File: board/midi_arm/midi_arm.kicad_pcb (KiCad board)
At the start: 2 copper layers, 100 x 100 mm, 25 parts, among them J1 Conn_01x02_Pin, J2 Conn_01x02_Pin, J3 Conn_01x10_Pin, J4 RJ45, J5 Conn_01x03_Pin, J6 Conn_01x03_Pin, J7 Conn_01x03_Pin, U6 6DOF_6050

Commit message: BABOI 2.0 Board
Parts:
- removed C1, C2, C3: 100nF, Capacitor_SMD:C_01005_0402Metric
- removed U2, U3, U4: ~, midi_arm:TOUCH_BAR
- added H7: MountingHole, MountingHole:MountingHole_2.2mm_M2, F.Cu at (127.5, 27.5)
- added H8: MountingHole, MountingHole:MountingHole_2.2mm_M2, F.Cu at (154.5, 27.5)
- added J10: Conn_01x01_Pin, Connector_PinHeader_1.27mm:PinHeader_1x01_P1.27mm_Vertical, F.Cu at (134.9, 47.5)
- added J8: Conn_01x06_Pin, GPB_Footprints:JST_1x6_2.54_cablepad, B.Cu at (134.8, 66.6)
- added J9: Conn_01x01_Pin, Connector_PinHeader_1.27mm:PinHeader_1x01_P1.27mm_Vertical, F.Cu at (131.6, 31.2)
- added R1: 2.4k, Resistor_SMD:R_0805_2012Metric_Pad1.20x1.40mm_HandSolder, B.Cu at (146.3, 37.5)
- added R10: 24k, Resistor_SMD:R_0805_2012Metric_Pad1.20x1.40mm_HandSolder, B.Cu at (148.3, 50.5)
- added R11: 2.4k, Resistor_SMD:R_0805_2012Metric_Pad1.20x1.40mm_HandSolder, B.Cu at (131.1, 37.3)
- added R12: 2.4k, Resistor_SMD:R_0805_2012Metric_Pad1.20x1.40mm_HandSolder, B.Cu at (128.9, 37.3)
- added R13: 2.4k, Resistor_SMD:R_0805_2012Metric_Pad1.20x1.40mm_HandSolder, B.Cu at (126.7, 37.3)
- added R14: 2.4k, Resistor_SMD:R_0805_2012Metric_Pad1.20x1.40mm_HandSolder, B.Cu at (133.3, 37.3)
- added R15: 24k, Resistor_SMD:R_0805_2012Metric_Pad1.20x1.40mm_HandSolder, B.Cu at (135.6, 37.3)
- added R16: 2.4k, Resistor_SMD:R_0805_2012Metric_Pad1.20x1.40mm_HandSolder, B.Cu at (133.6, 44.3)
- added R17: 2.4k, Resistor_SMD:R_0805_2012Metric_Pad1.20x1.40mm_HandSolder, B.Cu at (133.7, 50.7)
- added R18: 2.4k, Resistor_SMD:R_0805_2012Metric_Pad1.20x1.40mm_HandSolder, B.Cu at (126.9, 47.4)
- added R19: 2.4k, Resistor_SMD:R_0805_2012Metric_Pad1.20x1.40mm_HandSolder, B.Cu at (125.9, 44.5)
- added R2: 2.4k, Resistor_SMD:R_0805_2012Metric_Pad1.20x1.40mm_HandSolder, B.Cu at (155.5, 37.5)
- added R20: 24k, Resistor_SMD:R_0805_2012Metric_Pad1.20x1.40mm_HandSolder, B.Cu at (126.0, 50.5)
- added R3: 2.4k, Resistor_SMD:R_0805_2012Metric_Pad1.20x1.40mm_HandSolder, B.Cu at (148.5, 37.5)
- added R4: 2.4k, Resistor_SMD:R_0805_2012Metric_Pad1.20x1.40mm_HandSolder, B.Cu at (153.1, 37.5)
- added R5: 24k, Resistor_SMD:R_0805_2012Metric_Pad1.20x1.40mm_HandSolder, B.Cu at (150.8, 37.5)
- added R6: 2.4k, Resistor_SMD:R_0805_2012Metric_Pad1.20x1.40mm_HandSolder, B.Cu at (155.8, 50.6)
- added R7: 2.4k, Resistor_SMD:R_0805_2012Metric_Pad1.20x1.40mm_HandSolder, B.Cu at (154.9, 47.4)
- added R8: 2.4k, Resistor_SMD:R_0805_2012Metric_Pad1.20x1.40mm_HandSolder, B.Cu at (155.9, 44.4)
- added R9: 2.4k, Resistor_SMD:R_0805_2012Metric_Pad1.20x1.40mm_HandSolder, B.Cu at (148.3, 44.3)
- added RV1: R_Potentiometer_Small, midi_arm:pot_9.5x9.5, F.Cu at (137.4, 47.5)
- added RV2: R_Potentiometer_Small, midi_arm:pot_9.5x9.5, F.Cu at (141.0, 38.1)
- added RV3: R_Potentiometer_Small, midi_arm:pot_9.5x9.5, F.Cu at (144.5, 47.5)
- added RV4: R_Potentiometer_Small, midi_arm:pot_9.5x9.5, F.Cu at (141.0, 29.0)
- added SW1: SW_MEC_5E, GPB_Footprints:switch_Touchpad, F.Cu at (161.8, 38.6)
- added SW2: SW_MEC_5E, GPB_Footprints:switch_Touchpad, F.Cu at (161.8, 55.1)
- added SW3: SW_MEC_5E, GPB_Footprints:switch_Touchpad, F.Cu at (181.1, 38.6)
- added SW4: SW_MEC_5E, GPB_Footprints:switch_Touchpad, F.Cu at (181.1, 55.1)
- added U8: ~, midi_arm:ADS1115_mod, F.Cu at (124.6, 64.0)
- added U9: ~, Package_DIP:DIP-8_W7.62mm, F.Cu at (134.4, 33.8)
- J1: value Conn_01x02_Pin -> Conn_01x06_Pin; footprint Connector_PinHeader_2.54mm:PinHeader_1x02_P2.54mm_Vertical -> GPB_Footprints:JST_1x6_2.54
- J2: value Conn_01x02_Pin -> Conn_01x03_Pin; footprint Connector_PinHeader_2.54mm:PinHeader_1x02_P2.54mm_Vertical -> midi_arm:LED_conn; moved to B.Cu
- J3: value Conn_01x10_Pin -> Conn_01x08_Pin; footprint Connector_PinHeader_2.54mm:PinHeader_1x10_P2.54mm_Vertical -> Connector_PinHeader_2.54mm:PinHeader_1x08_P2.54mm_Vertical
- J4: value RJ45 -> Conn_01x05_Pin; footprint Connector_RJ:RJ45_Ninigi_GE -> GPB_Footprints:JST_1x5_2.54_cablepad; moved to B.Cu
- J5, J6, J7: value Conn_01x03_Pin -> Conn_01x01_Pin; footprint Connector_PinHeader_2.54mm:PinHeader_1x03_P2.54mm_Vertical -> Connector_PinHeader_1.27mm:PinHeader_1x01_P1.27mm_Vertical
- U1: footprint midi_arm:Wemos_S3_Mini_Outer_Pins -> GPB_Footprints:ESP32_S2_Wemos_Mini
- U7: footprint midi_arm:TOUCH_BAR -> Package_DIP:DIP-8_W7.62mm
- moved H2 98.6 mm to (187.5, 27.5)
- moved H4 98.4 mm to (187.5, 122.5)
- moved H6 61.1 mm to (127.5, 70.4)
- moved U7 44.2 mm to (147.6, 41.4), turned to 90 degrees
- moved J1 43.3 mm to (180.3, 26.7), turned to -90 degrees
- moved U6 36.4 mm to (138.7, 53.8)
- moved J5 36.1 mm to (129.2, 53.7)
- moved J4 35.0 mm to (146.1, 31.4), turned to 90 degrees
- moved H1 33.6 mm to (160.6, 27.5)
- moved D2 31.1 mm to (185.5, 33.9)
- moved D1 31.0 mm to (162.4, 33.9), turned to 0 degrees
- moved J2 29.6 mm to (181.6, 35.6), turned to 90 degrees
- moved H3 27.1 mm to (160.5, 122.5)
- moved H5 15.9 mm to (154.5, 70.4)
- moved U1 13.7 mm to (162.6, 97.8), turned to 0 degrees
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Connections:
- J1 pad 1: /VBUS -> GND1
- J1 pad 2: /VBUS -> /INT
- J2 pad 1: Net-(J2-Pin_1) -> GND1
- J2 pad 2: Net-(J2-Pin_1) -> Net-(D2-DOUT)
- J3 pad 2: Net-(D2-DOUT) -> /EXT_D0
- J3 pad 3: Net-(J3-Pin_3) -> /EXT_D1
- J3 pad 4: Net-(J3-Pin_4) -> /EXT_D2
- J3 pad 5: Net-(J3-Pin_5) -> /EXT_D3
- J3 pad 6: Net-(J3-Pin_6) -> /EXT_INT
- J3 pad 7: Net-(J3-Pin_7) -> /VBUS
- J3 pad 8: Net-(J3-Pin_8) -> /VCC_3V3
- J4 pad 1: Net-(J5-Pin_1) -> Net-(J4-Pin_1)
- J4 pad 2: Net-(U6-SCL) -> Net-(J4-Pin_2)
- J4 pad 3: Net-(U6-SDA) -> Net-(J4-Pin_3)
- J4 pad 4: Net-(J7-Pin_2) -> Net-(J4-Pin_4)
- J4 pad 5: Net-(J6-Pin_2) -> GND2
- J5 pad 1: Net-(J5-Pin_1) -> GND2
- J6 pad 1: Net-(J5-Pin_1) -> Net-(J6-Pin_1)
- J7 pad 1: Net-(J5-Pin_1) -> Net-(J7-Pin_1)
- U5 pad 1: Net-(J2-Pin_1) -> /VCC_3V3
- U5 pad 3: Net-(U1-5) -> /SCL
- U5 pad 4: Net-(U1-7) -> /SDA
- U5 pad 8: unconnected-(U5-INT-Pad8) -> Net-(U1-GPIO_18)
- U6 pad 1: Net-(J5-Pin_3) -> /GLOVE_VCC
- U6 pad 2: Net-(J5-Pin_1) -> GND2
- U6 pad 3: Net-(U6-SCL) -> /GLOVE_SCL
- U6 pad 4: Net-(U6-SDA) -> /GLOVE_SDA
- U6 pad 8: unconnected-(U6-INT-Pad8) -> /GLOVE_ACC_INT
- U7 pad 1: Net-(U7-DOUT) -> Net-(U7-VoutA)
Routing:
- net /VCC_3V3: track 0.00 -> 136.2 mm
- net /GLOVE_VCC: track 0.00 -> 134.5 mm, vias 0 -> 2
- net GND2: track 0.00 -> 132.1 mm
- net GND1: track 83.2 -> 201.1 mm, vias 3 -> 2
- net Net-(U1-GPIO_10): track 0.00 -> 102.4 mm, vias 0 -> 1
- net /EXT_SCL: track 0.00 -> 101.1 mm, vias 0 -> 2
- net Net-(U1-GPIO_2): track 0.00 -> 92.6 mm
- net /ALERT: track 0.00 -> 89.4 mm, vias 0 -> 2
- net /INT: track 0.00 -> 88.7 mm, vias 0 -> 1
- net /EXT_SDA: track 0.00 -> 86.5 mm, vias 0 -> 1
- net Net-(U1-GPIO_3): track 0.00 -> 84.5 mm
- net Net-(U1-GPIO_9): track 0.00 -> 78.8 mm, vias 0 -> 1
- net Net-(J2-Pin_1): track 78.1 -> 0.00 mm
- net Net-(U1-3): track 60.9 -> 0.00 mm
- net Net-(U1-11): track 60.5 -> 0.00 mm
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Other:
- board text added: "(C) '23/'24 Michael Hartmann"
- board text added: "(C)'23 M. Hartmann"
- board text added: "A"
- board text added: "B"
- board text added: "BABOI V2.0"
- board text added: "C"
- board text added: "Glove Board"
- board text added: "S"
- board text removed: "(C) 2023"
- board text removed: "BABOI"
- board text removed: "MHARTMANN"
- board text removed: "V 1.0"

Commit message: Updates
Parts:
- turned R3 to 90 degrees
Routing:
- net Net-(J7-Pin_1): track 38.2 -> 24.5 mm, vias 0 -> 2
- net Net-(R1-Pad2): track 0.00 -> 11.4 mm, vias 0 -> 2
- net Net-(U7-VoutA): track 43.9 -> 36.7 mm, vias 3 -> 1
- net GND2: track 132.1 -> 125.4 mm, vias 0 -> 1
- net Net-(J6-Pin_1): track 24.6 -> 30.0 mm
- net Net-(U7-VinA-): track 13.4 -> 8.83 mm, vias 1 -> 0
- net Net-(R11-Pad2): track 5.20 -> 7.44 mm
- net /GLOVE_VCC: track 134.5 -> 133.0 mm
- net Net-(U7-VinB-): track 23.4 -> 22.1 mm

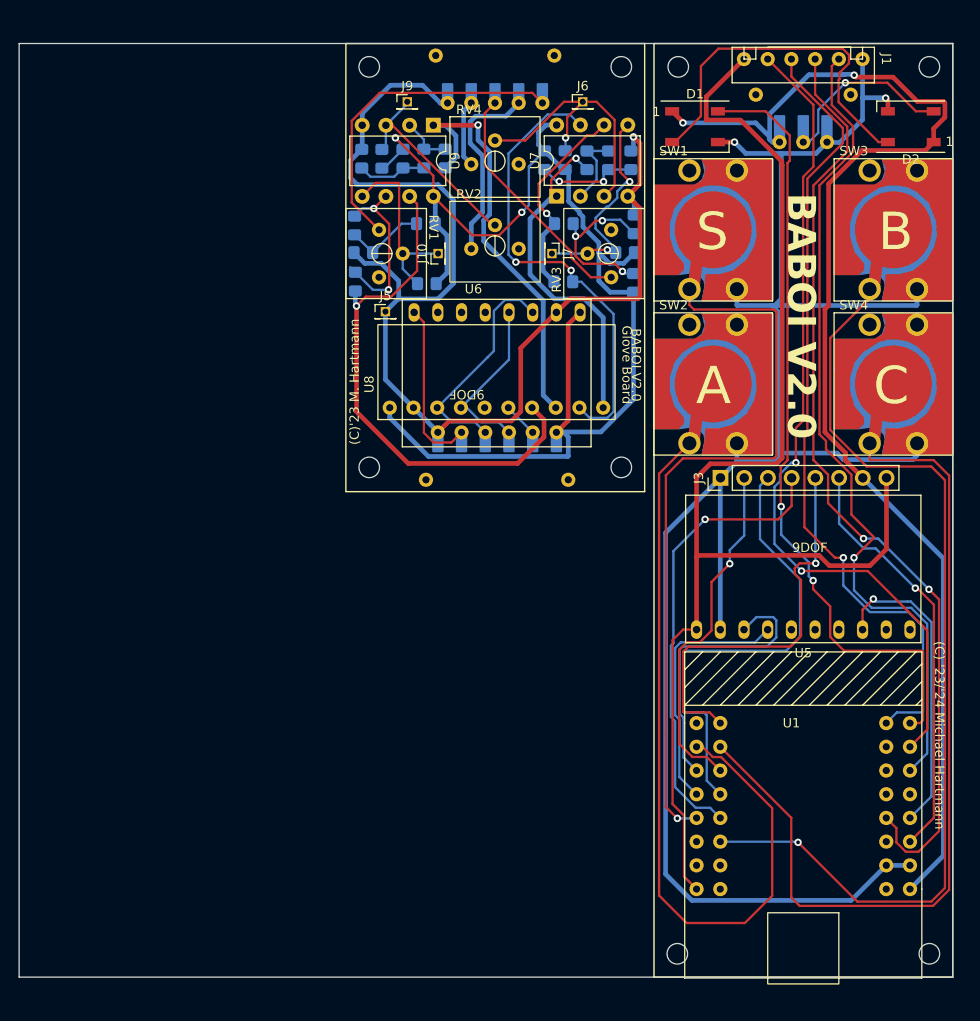
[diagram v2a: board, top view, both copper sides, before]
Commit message: HW Version 3 Support
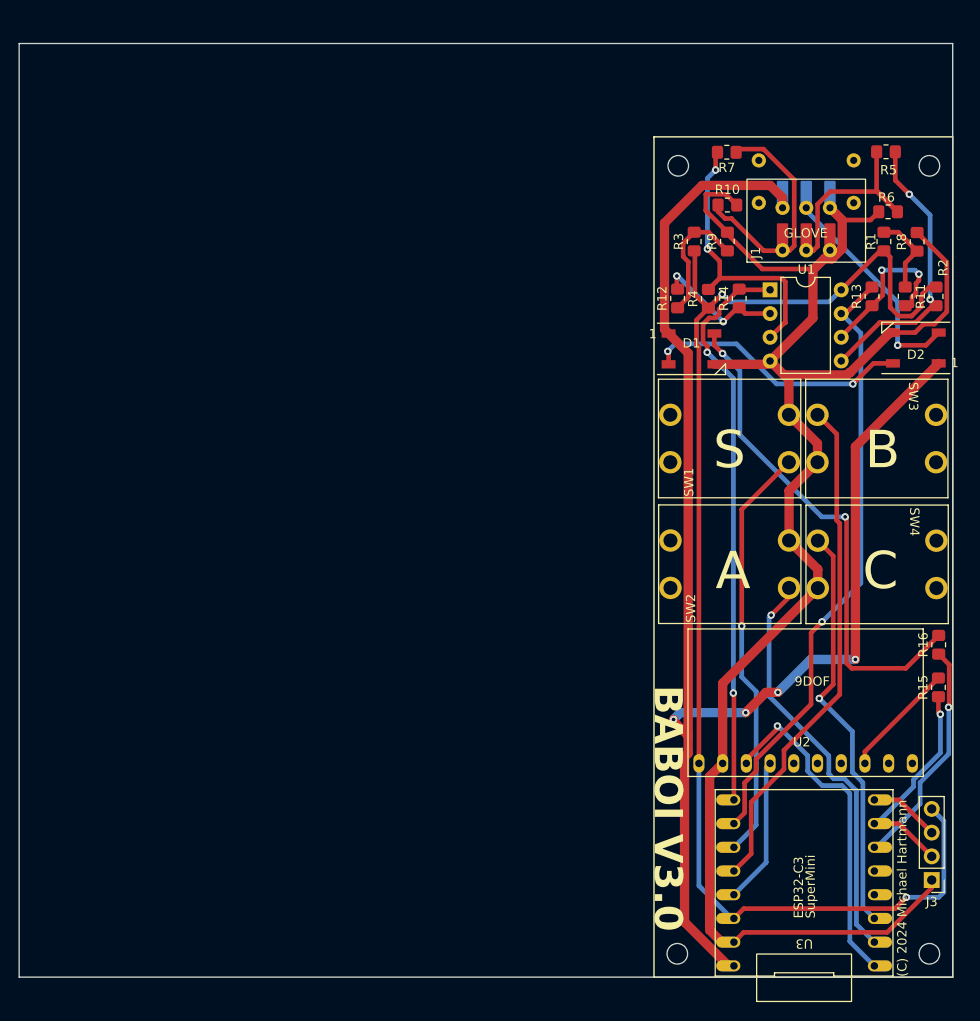
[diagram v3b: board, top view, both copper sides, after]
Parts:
- removed H5, H6, H7, H8: MountingHole, MountingHole:MountingHole_2.2mm_M2
- removed J10, J5, J6, J7, J9: Conn_01x01_Pin, Connector_PinHeader_1.27mm:PinHeader_1x01_P1.27mm_Vertical
- removed J4: Conn_01x05_Pin, GPB_Footprints:JST_1x5_2.54_cablepad
- removed J8: Conn_01x06_Pin, GPB_Footprints:JST_1x6_2.54_cablepad
- removed R17, R18, R19: 2.4k, Resistor_SMD:R_0805_2012Metric_Pad1.20x1.40mm_HandSolder
- removed R20: 24k, Resistor_SMD:R_0805_2012Metric_Pad1.20x1.40mm_HandSolder
- removed RV1, RV2, RV3, RV4: R_Potentiometer_Small, midi_arm:pot_9.5x9.5
- removed U5: ~, midi_arm:9250_MOD
- removed U6: 6DOF_6050, midi_arm:6050_MOD
- removed U7, U9: ~, Package_DIP:DIP-8_W7.62mm
- removed U8: ~, midi_arm:ADS1115_mod
- added U2: ~, midi_arm:9250_MOD, F.Cu at (174.2, 102.1)
- added U3: ~, midi_arm:ESP32-C3_SuperMini, F.Cu at (174.1, 114.9)
- J1: value Conn_01x06_Pin -> Conn_01x03_Pin; footprint GPB_Footprints:JST_1x6_2.54 -> midi_arm:LED_conn
- J3: value Conn_01x08_Pin -> Conn_01x04_Pin; footprint Connector_PinHeader_2.54mm:PinHeader_1x08_P2.54mm_Vertical -> Connector_PinHeader_2.54mm:PinHeader_1x04_P2.54mm_Vertical
- R1, R15, R3: moved to F.Cu
- R10, R5: value 24k -> 3.3k; moved to F.Cu
- R11, R12, R6, R7, R8, R9: value 2.4k -> 3.3k; moved to F.Cu
- R13, R14, R16: value 2.4k -> 24k; moved to F.Cu
- R2, R4: value 2.4k -> 5.1k; moved to F.Cu
- SW1, SW2, SW3, SW4: footprint GPB_Footprints:switch_Touchpad -> GPB_Footprints:switch_Simple
- U1: footprint GPB_Footprints:ESP32_S2_Wemos_Mini -> Package_DIP:DIP-8_W7.62mm
- moved R15 77.5 mm to (188.5, 94.0), turned to 90 degrees
- moved R16 71.1 mm to (188.5, 89.4), turned to 90 degrees
- moved R13 56.6 mm to (181.4, 52.1)
- moved R11 55.8 mm to (184.9, 52.1)
- moved J3 48.7 mm to (187.8, 114.6), turned to 180 degrees
- moved U1 47.1 mm to (170.4, 51.4)
- moved R1 37.4 mm to (182.6, 46.2), turned to 90 degrees
- moved R14 37.0 mm to (167.1, 52.3)
- moved R2 35.8 mm to (188.2, 52.1), turned to -90 degrees
- moved R12 35.0 mm to (160.5, 52.3)
- moved R5 32.0 mm to (182.8, 36.6), turned to 0 degrees
- moved SW1 31.3 mm to (159.8, 69.8), turned to 90 degrees
- moved R8 30.4 mm to (186.2, 46.2)
- moved R6 28.3 mm to (183.1, 43.0), turned to 180 degrees
- moved SW2 28.3 mm to (159.8, 83.3), turned to 90 degrees
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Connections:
- J1 pad 1: GND1 -> Net-(J1-Pin_1)
- J1 pad 2: /INT -> Net-(J1-Pin_2)
- J1 pad 3: /EXT_SCL -> GND1
- J3 pad 2: /EXT_D0 -> Net-(J3-Pin_2)
- J3 pad 3: /EXT_D1 -> Net-(J3-Pin_3)
- J3 pad 4: /EXT_D2 -> /VCC_3V3
- R1 pad 1: /GLOVE_VCC -> /VCC_3V3
- R10 pad 1: Net-(U7-VinB-) -> Net-(J1-Pin_1)
- R10 pad 2: Net-(U7-VoutB) -> GND1
- R11 pad 1: /GLOVE_VCC -> Net-(R1-Pad2)
- R11 pad 2: Net-(R11-Pad2) -> Net-(U1-VinB-)
- R12 pad 1: /GLOVE_VCC -> Net-(R12-Pad1)
- R12 pad 2: Net-(J9-Pin_1) -> Net-(U1-VinA-)
- R13 pad 1: Net-(R11-Pad2) -> Net-(U1-VinB-)
- R13 pad 2: GND2 -> /ADC1_1
- R14 pad 1: Net-(R11-Pad2) -> Net-(U1-VinA-)
- R14 pad 2: Net-(U9-VinA-) -> /ADC1_0
- R15 pad 1: Net-(U9-VinA-) -> Net-(J3-Pin_2)
- R16 pad 1: /GLOVE_VCC -> Net-(U3-GPIO10)
- R16 pad 2: Net-(R16-Pad2) -> Net-(D1-DIN)
- R2 pad 1: Net-(R1-Pad2) -> /VCC_3V3
- R2 pad 2: GND2 -> Net-(U1-VinB+)
- R3 pad 1: /GLOVE_VCC -> /VCC_3V3
- R3 pad 2: Net-(J6-Pin_1) -> Net-(R12-Pad1)
- R4 pad 1: Net-(R1-Pad2) -> /VCC_3V3
- R4 pad 2: Net-(U7-VinA-) -> Net-(U1-VinA+)
- R5 pad 1: Net-(U7-VinA-) -> Net-(J1-Pin_2)
- R5 pad 2: Net-(U7-VoutA) -> Net-(U1-VinB+)
- R6 pad 1: /GLOVE_VCC -> Net-(J1-Pin_2)
- R6 pad 2: Net-(R6-Pad2) -> GND1
- R7 pad 1: /GLOVE_VCC -> Net-(J1-Pin_1)
- R7 pad 2: Net-(J7-Pin_1) -> Net-(U1-VinA+)
- R8 pad 1: Net-(R6-Pad2) -> Net-(R1-Pad2)
- R8 pad 2: GND2 -> GND1
- R9 pad 1: Net-(R6-Pad2) -> Net-(R12-Pad1)
- R9 pad 2: Net-(U7-VinB-) -> GND1
- SW1 pad 2: Net-(U1-GPIO_9) -> /BUTTON1
- SW2 pad 2: Net-(U1-GPIO_3) -> /BUTTON3
- SW3 pad 2: Net-(U1-GPIO_10) -> /BUTTON2
- SW4 pad 2: Net-(U1-GPIO_2) -> /BUTTON4
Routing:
- net /GLOVE_VCC: track 133.0 -> 0.00 mm, vias 2 -> 0
- net GND2: track 125.4 -> 0.00 mm, vias 1 -> 0
- net Net-(U1-GPIO_10): track 102.4 -> 0.00 mm, vias 1 -> 0
- net /EXT_SCL: track 101.1 -> 0.00 mm, vias 2 -> 0
- net Net-(U1-GPIO_2): track 92.6 -> 0.00 mm
- net /ALERT: track 89.4 -> 0.00 mm, vias 2 -> 0
- net /INT: track 88.7 -> 0.00 mm, vias 1 -> 0
- net /EXT_SDA: track 86.5 -> 0.00 mm, vias 1 -> 0
- net Net-(U1-GPIO_3): track 84.5 -> 0.00 mm
- net Net-(U1-GPIO_9): track 78.8 -> 0.00 mm, vias 1 -> 0
- net /ADC1_1: track 0.00 -> 65.6 mm, vias 0 -> 1
- net /ADC1_0: track 0.00 -> 61.4 mm, vias 0 -> 2
- net Net-(U8-A0): track 56.6 -> 0.00 mm, vias 1 -> 0
- net /BUTTON2: track 0.00 -> 54.6 mm
- net /EXT_D1: track 50.4 -> 0.00 mm
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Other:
- board text added: "(C) 2024 Michael Hartmann"
- board text added: "BABOI V3.0"
- board text added: "GLOVE"
- board text added: "LED"
- board text removed: "(C) '23/'24 Michael Hartmann"
- board text removed: "(C)'23 M. Hartmann"
- board text removed: "BABOI V2.0"
- board text removed: "Glove Board"

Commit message: Board 3.5 and code cleanup
Mini version of Baboi
Remove Tension Strip option 3/4
Remove  Option for Touch pads
Move light control to host software
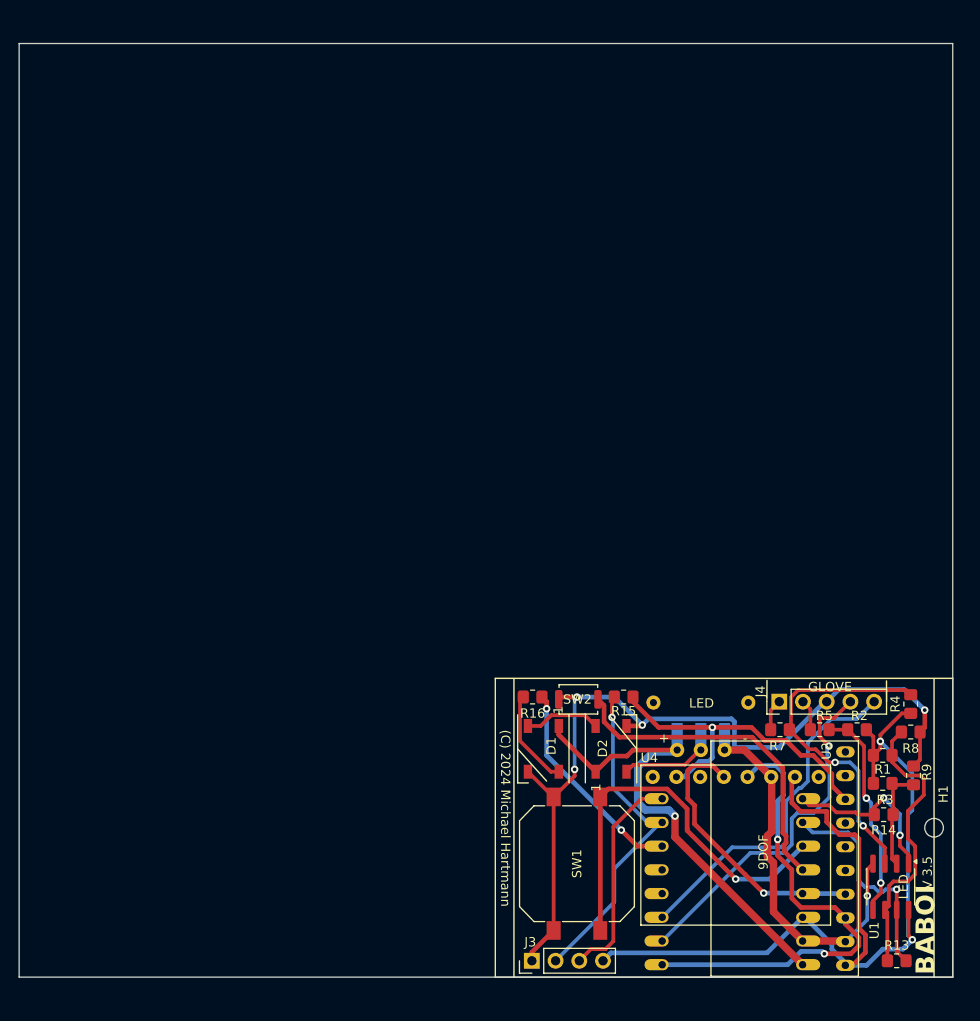
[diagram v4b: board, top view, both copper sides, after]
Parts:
- removed H2, H3, H4: MountingHole, MountingHole:MountingHole_2.2mm_M2
- removed J1: Conn_01x03_Pin, midi_arm:LED_conn
- removed R10, R11, R12, R6: 3.3k, Resistor_SMD:R_0805_2012Metric_Pad1.20x1.40mm_HandSolder
- removed SW3, SW4: SW_MEC_5E, GPB_Footprints:switch_Simple
- added J4: Conn_01x05_Pin, Connector_PinHeader_2.54mm:PinHeader_1x05_P2.54mm_Vertical, F.Cu at (171.4, 95.5)
- added U4: ~, midi_arm:GY-85, F.Cu at (180.7, 103.6)
- H1: footprint MountingHole:MountingHole_2.2mm_M2 -> MountingHole:MountingHole_2mm
- R1, R3: value 2.4k -> 33K
- R13, R14: value 24k -> 51K
- R15: value 24k -> 0k
- R16: value 24k -> 24K
- R2, R4: value 5.1k -> 33K
- R5, R7: value 3.3k -> 10K
- R8, R9: value 3.3k -> 33K
- SW1: footprint GPB_Footprints:switch_Simple -> midi_arm:SW_Push_SMD
- SW2: value SW_MEC_5E -> SW_DIP_x01; footprint GPB_Footprints:switch_Simple -> Button_Switch_SMD:SW_Push_SPST_NO_Alps_SKRK
- U1: footprint Package_DIP:DIP-8_W7.62mm -> Package_SO:SOIC-8_3.9x4.9mm_P1.27mm
- U3: moved to B.Cu
- moved H1 76.0 mm to (188.0, 109.0)
- moved R13 71.2 mm to (184.0, 123.2), turned to 0 degrees
- moved U1 65.2 mm to (183.4, 115.3), turned to -90 degrees
- moved R5 62.3 mm to (175.8, 98.5)
- moved R7 62.1 mm to (171.5, 98.5), turned to 0 degrees
- moved R3 61.5 mm to (182.5, 104.2), turned to 0 degrees
- moved R9 60.6 mm to (185.8, 103.4)
- moved J2 59.2 mm to (170.6, 100.7)
- moved R14 57.4 mm to (182.6, 107.6), turned to 180 degrees
- moved R1 55.0 mm to (182.5, 101.2), turned to 0 degrees
- moved D2 53.9 mm to (153.4, 100.5), turned to 90 degrees
- moved R8 52.5 mm to (185.5, 98.8), turned to 0 degrees
- moved R4 48.5 mm to (185.5, 95.8)
- moved R2 47.2 mm to (179.8, 98.5), turned to 180 degrees
- moved D1 45.7 mm to (146.2, 100.5), turned to -90 degrees
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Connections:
- R1 pad 2: Net-(R1-Pad2) -> Net-(U1-VinB-)
- R3 pad 2: Net-(R12-Pad1) -> Net-(U1-VinA-)
- R8 pad 1: Net-(R1-Pad2) -> Net-(U1-VinB-)
- R9 pad 1: Net-(R12-Pad1) -> Net-(U1-VinA-)
- SW1 pad 1: unconnected-(SW1-Pad1) -> /BUTTON1
- SW1 pad 2: /BUTTON1 -> GND1
- SW2 pad 1: unconnected-(SW2-Pad1) -> /BUTTON2
- SW2 pad 2: /BUTTON3 -> GND1
- U3 pad 10: /BUTTON3 -> /SPARE1
- U3 pad 11: /BUTTON4 -> /SPARE2
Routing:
- net /VBUS: track 159.2 -> 51.1 mm, vias 4 -> 1
- net GND1: track 180.3 -> 130.1 mm, vias 0 -> 5
- net /BUTTON4: track 44.2 -> 0.00 mm, vias 1 -> 0
- net /BUTTON3: track 44.2 -> 0.00 mm, vias 1 -> 0
- net Net-(D1-DIN): track 54.2 -> 10.4 mm, vias 2 -> 0
- net /ADC1_0: track 61.4 -> 18.8 mm
- net /ADC1_1: track 65.6 -> 24.3 mm
- net /SPARE1: track 0.00 -> 39.3 mm, vias 0 -> 1
- net /VCC_3V3: track 143.2 -> 105.5 mm
- net /SPARE2: track 0.00 -> 37.3 mm
- net Net-(U2-INT): track 12.4 -> 35.8 mm, vias 0 -> 1
- net Net-(J4-Pin_1): track 25.6 -> 3.38 mm
- net Net-(D1-DOUT): track 28.6 -> 8.20 mm, vias 2 -> 0
- net Net-(J4-Pin_2): track 23.3 -> 3.33 mm
- net /BUTTON2: track 54.6 -> 35.8 mm
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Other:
- board text added: "+"
- board text added: "-"
- board text added: "BABOI"
- board text added: "V 3.5"
- board text removed: "A"
- board text removed: "B"
- board text removed: "BABOI V3.0"
- board text removed: "C"
- board text removed: "S"
